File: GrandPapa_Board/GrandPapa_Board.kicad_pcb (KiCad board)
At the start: 4 copper layers, 82 x 82 mm, 98 parts, among them J1 3.7V LiPo Single Cell, J11 Dupont 01x04_Male, J2 HARWIN_ROCKET, J3 Dupont_GPS, J4 HARWIN_MINISENSOR, J5 Dupont_Logger, J6 PROG Header, J7 HARWIN_KALMAN, J8 Therm EN Jumper, U1 MCP1642B-50I/MS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

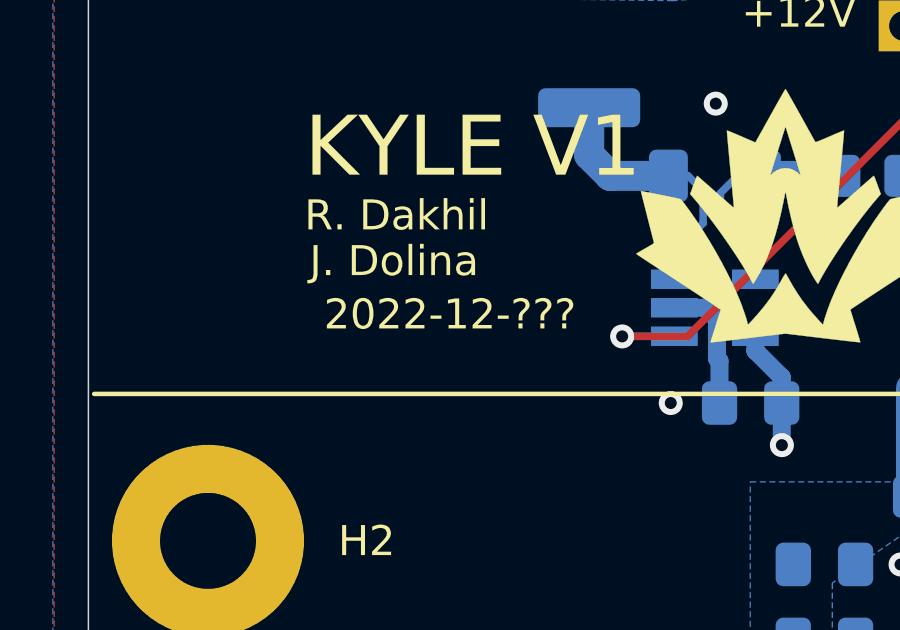
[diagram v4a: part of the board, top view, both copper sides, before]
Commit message: Finalize date on sikscreen; regen gerbers
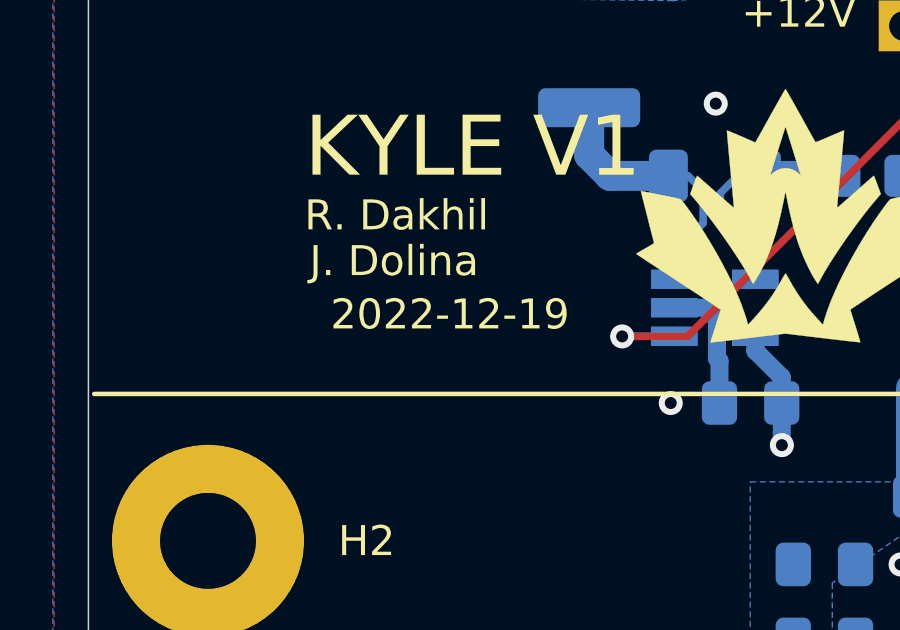
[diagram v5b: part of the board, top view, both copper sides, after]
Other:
- board text added: "2022-12-19"
- board text removed: "2022-12-???"
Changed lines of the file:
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@@
     (effects (font (size 0.6 0.6) (thickness 0.15)))
   )
-  (gr_text "2022-12-???" (at 125.350433 80.49237) (layer "F.SilkS")
+  (gr_text "2022-12-19" (at 125.350433 80.49237) (layer "F.SilkS")
     (effects (font (size 1 1) (thickness 0.15)))
   )
